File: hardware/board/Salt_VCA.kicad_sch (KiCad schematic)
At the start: 40 parts

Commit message: hardware: clear ERC issues, move BCM847 to the Winterbloom symbol library
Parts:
- Q?: symbol Carson's Schematic Symbols:BCM847 -> winterbloom:BCM847
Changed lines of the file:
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@@
     )
   )
-  (symbol (lib_name "BCM847_1") (lib_id "Carson's Schematic Symbols:BCM847") (at 161.29 140.97 270) (unit 1)
+  (symbol (lib_id "winterbloom:BCM847") (at 161.29 140.97 270) (unit 1)
     (in_bom yes) (on_board yes) (dnp no)
     (property "Reference" "Q?" (at 149.225 132.08 90)
@@
       (effects (font (size 1.27 1.27)) (justify left))
     )
-    (property "Footprint" "Package_TO_SOT_SMD:SOT-363_SC-70-6" (at 173.355 140.97 0)
+    (property "Footprint" "Package_TO_SOT_SMD:SOT-363_SC-70-6" (at 161.29 140.97 0)
       (effects (font (size 1.27 1.27)) hide)
     )
-    (property "Datasheet" "" (at 173.355 140.97 0)
+    (property "Datasheet" "https://assets.nexperia.com/documents/data-sheet/BCM847BS.pdf" (at 161.29 140.97 0)
       (effects (font (size 1.27 1.27)) hide)
     )

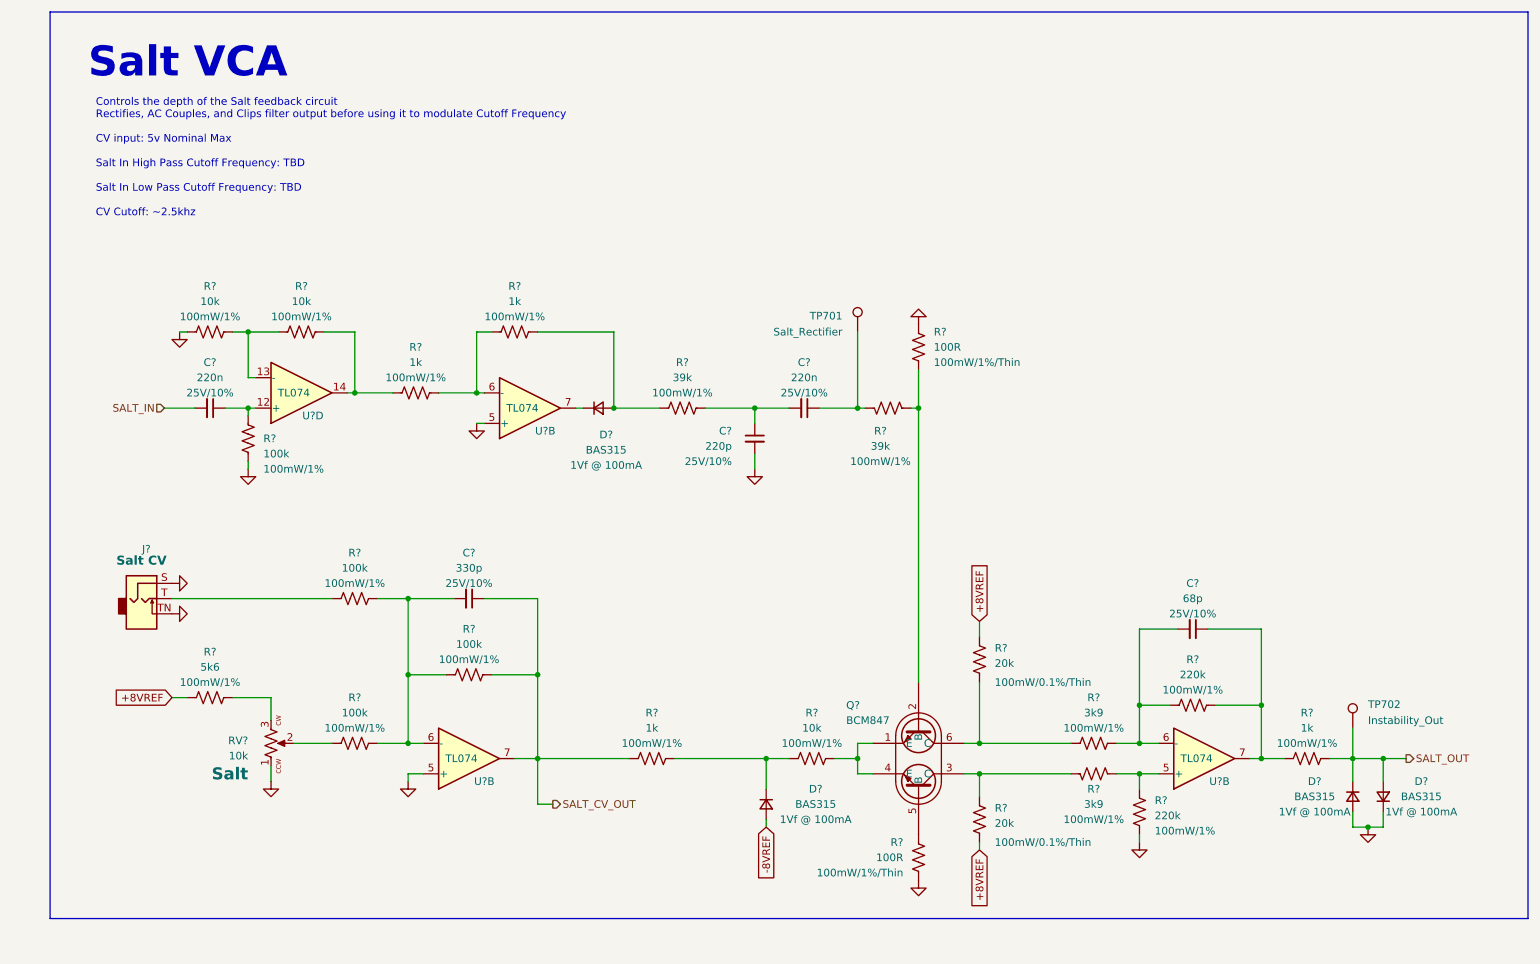
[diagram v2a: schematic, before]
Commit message: hardware: add MPNs, DigiKey part numbers, and LCSC part numbers for all BOM items
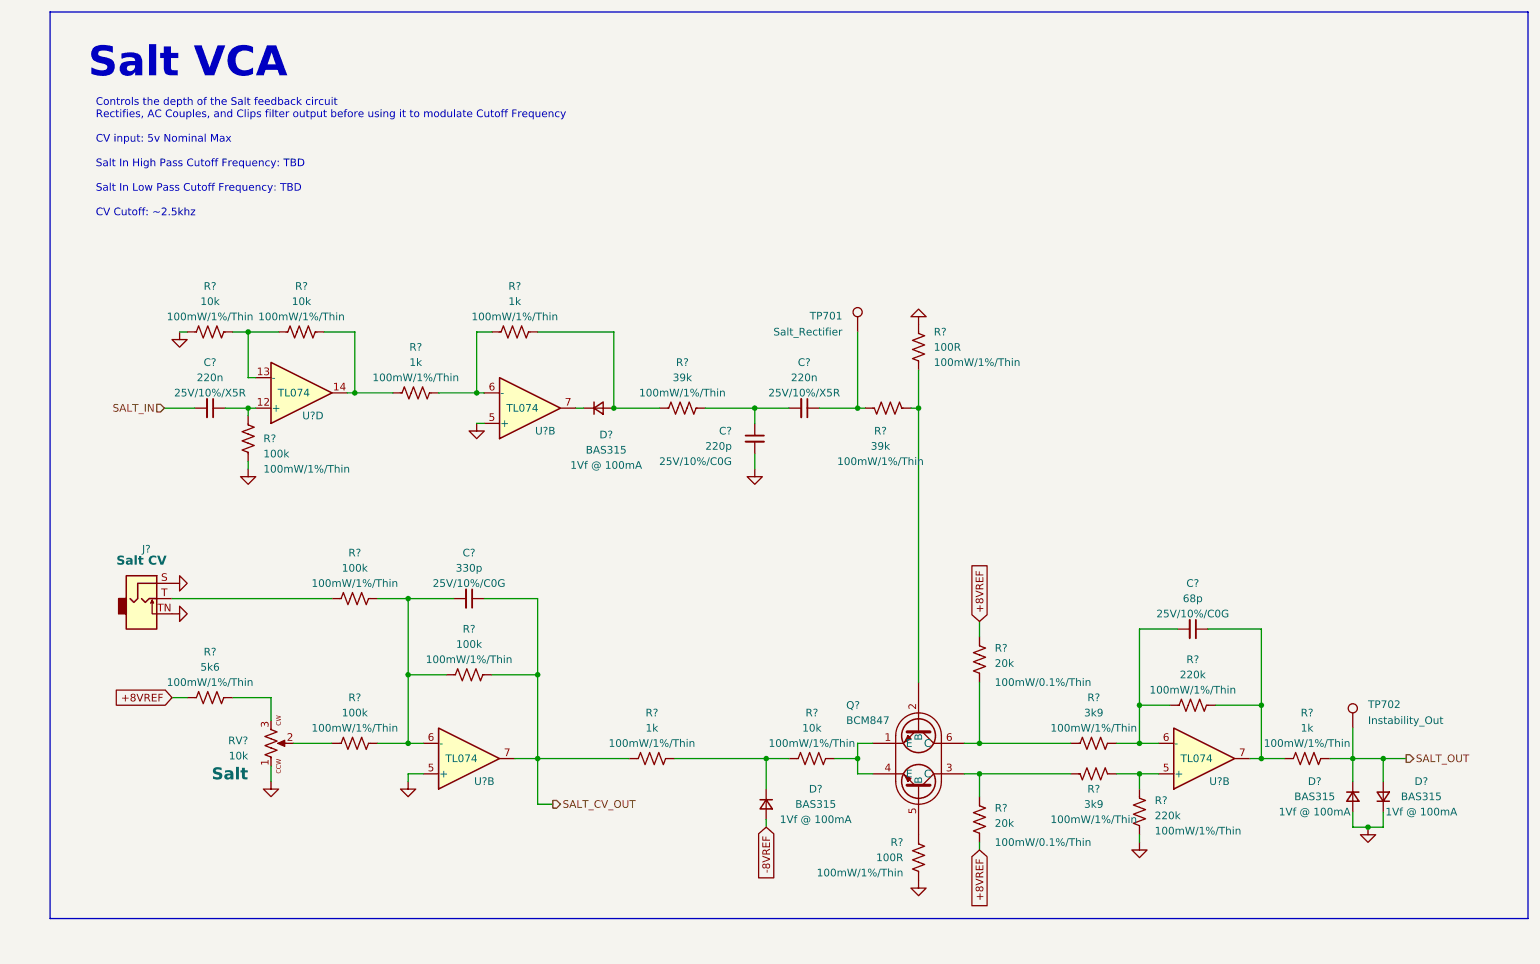
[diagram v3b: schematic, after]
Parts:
- C? (x2): DigiKey (none) -> 1276-1876-1-ND; LCSC (none) -> C307462; MPN (none) -> CL10A224KB8NNNC; Rating 25V/10% -> 25V/10%/X5R; Substitutes Allowed (none) -> Yes
- C?: DigiKey (none) -> 1276-1073-1-ND; LCSC (none) -> C1664; MPN (none) -> CL10C331JB8NNNC; Rating 25V/10% -> 25V/10%/C0G; Substitutes Allowed (none) -> Yes
- C?: DigiKey (none) -> 1276-1135-1-ND; LCSC (none) -> C28262; MPN (none) -> CL10C680JB8NNNC; Rating 25V/10% -> 25V/10%/C0G; Substitutes Allowed (none) -> Yes
- C?: DigiKey (none) -> 1276-1048-1-ND; LCSC (none) -> C27675; MPN (none) -> CL10C221JB8NNNC; Rating 25V/10% -> 25V/10%/C0G; Substitutes Allowed (none) -> Yes
- D? (x4): DigiKey (none) -> 1727-4309-2-ND; LCSC (none) -> C109218; Substitutes Allowed (none) -> No
- Q?: Attention ! -> (none); DigiKey (none) -> 1727-5456-1-ND; LCSC (none) -> C396099; Substitutes Allowed (none) -> No
- R? (x3): DigiKey (none) -> YAG2321CT-ND; LCSC (none) -> C469659; MPN (none) -> RT0603FRE0710KL; Rating 100mW/1% -> 100mW/1%/Thin; Substitutes Allowed (none) -> Yes
- R? (x2): DigiKey (none) -> YAG1582CT-ND; LCSC (none) -> C723637; MPN (none) -> RT0603BRD0720KL; Substitutes Allowed (none) -> Ask
- R? (x2): DigiKey (none) -> YAG1497CT-ND; LCSC (none) -> C122970; MPN (none) -> RT0603BRD07100RL; Substitutes Allowed (none) -> Ask
- R? (x2): DigiKey (none) -> YAG5961CT-ND; LCSC (none) -> C863790; MPN (none) -> RT0603FRE073K9L; Rating 100mW/1% -> 100mW/1%/Thin; Substitutes Allowed (none) -> Yes
- R? (x4): DigiKey (none) -> 13-RT0603FRE13100KLTR-ND; LCSC (none) -> C4107493; MPN (none) -> RT0603FRE13100KL; Rating 100mW/1% -> 100mW/1%/Thin; Substitutes Allowed (none) -> Yes
- R? (x4): DigiKey (none) -> YAG2323TR-ND; LCSC (none) -> C375503; MPN (none) -> RT0603FRE071KL; Rating 100mW/1% -> 100mW/1%/Thin; Substitutes Allowed (none) -> Yes
- R? (x2): DigiKey (none) -> 13-RT0603FRE0739KLCT-ND; LCSC (none) -> C706166; MPN (none) -> RT0603FRE0739KL; Rating 100mW/1% -> 100mW/1%/Thin; Substitutes Allowed (none) -> Yes
- R?: DigiKey (none) -> 13-RT0603FRE075K6LCT-ND; LCSC (none) -> C706186; MPN (none) -> RT0603FRE075K6L; Rating 100mW/1% -> 100mW/1%/Thin; Substitutes Allowed (none) -> Yes
- R? (x2): DigiKey (none) -> YAG5946CT-ND; LCSC (none) -> C706140; MPN (none) -> RT0603FRE07220KL; Rating 100mW/1% -> 100mW/1%/Thin; Substitutes Allowed (none) -> Yes
- U? (x4): DigiKey (none) -> 296-7198-1-ND; LCSC (none) -> C96507; MPN TL074CPW -> TL074CPWR; Substitutes Allowed (none) -> No

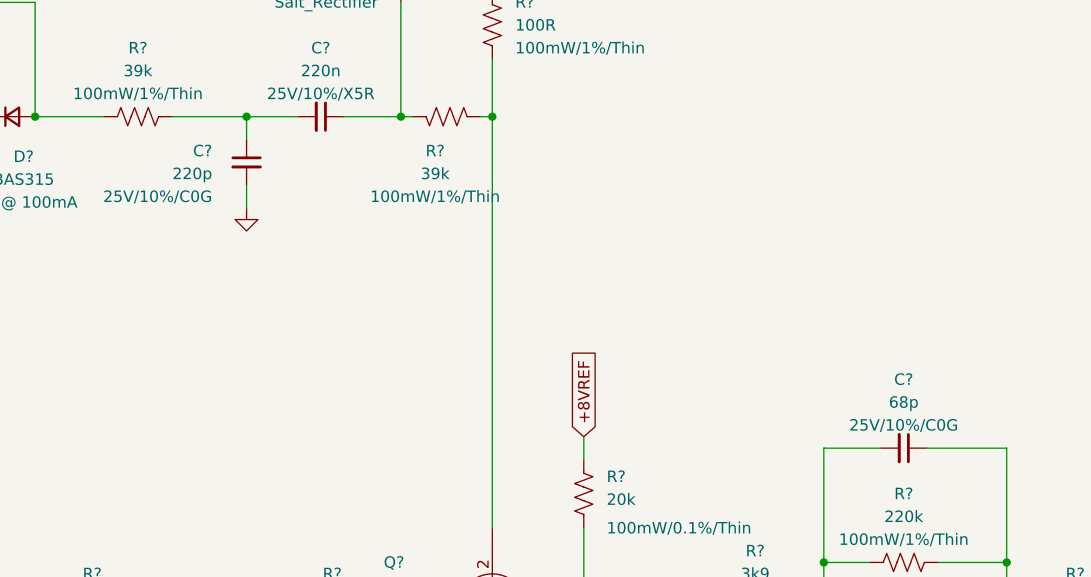
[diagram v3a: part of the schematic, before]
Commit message: hardware: change C702 from 220pF to 330pF and  C705 from 68pF to 100pF to reduce unique values
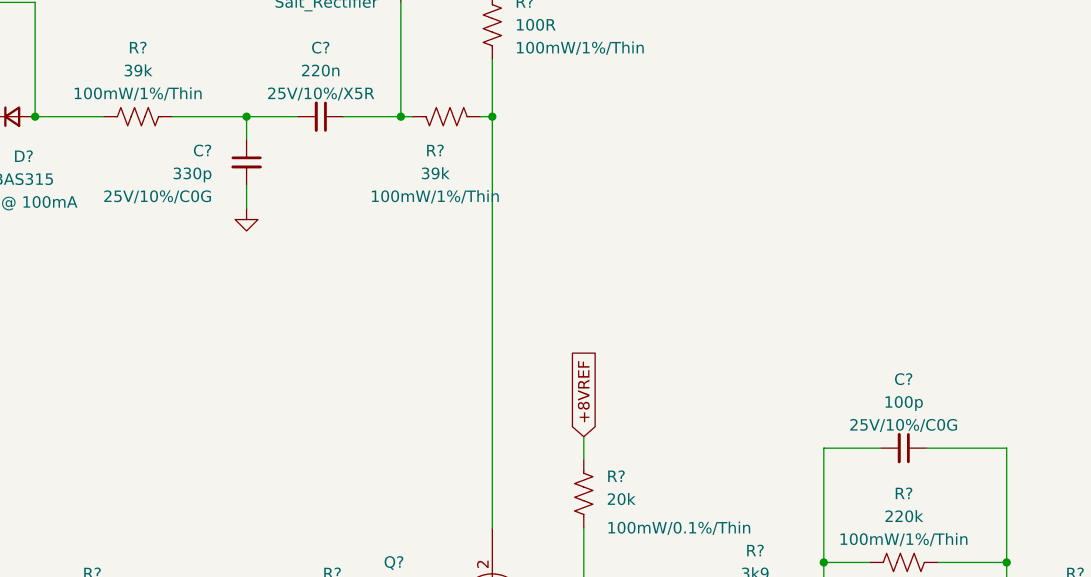
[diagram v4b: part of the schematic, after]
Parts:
- C?: value 68p -> 100p; DigiKey 1276-1135-1-ND -> 1276-1008-1-ND; LCSC C28262 -> C14858; MPN CL10C680JB8NNNC -> CL10C101JB8NNNC
- C?: value 220p -> 330p; DigiKey 1276-1048-1-ND -> 1276-1073-1-ND; LCSC C27675 -> C1664; MPN CL10C221JB8NNNC -> CL10C331JB8NNNC
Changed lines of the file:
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@@
       (effects (font (size 1.27 1.27)))
     )
-    (property "Value" "68p" (at 207.0036 114.3 90)
+    (property "Value" "100p" (at 207.0036 114.3 90)
       (effects (font (size 1.27 1.27)))
     )
@@
       (effects (font (size 1.27 1.27)))
     )
-    (property "DigiKey" "1276-1135-1-ND" (at 207.01 119.38 0)
-      (effects (font (size 1.27 1.27)) hide)
-    )
-    (property "LCSC" "C28262" (at 207.01 119.38 0)
+    (property "DigiKey" "1276-1008-1-ND" (at 207.01 119.38 0)
+      (effects (font (size 1.27 1.27)) hide)
+    )
+    (property "LCSC" "C14858" (at 207.01 119.38 0)
       (effects (font (size 1.27 1.27)) hide)
     )
@@
       (effects (font (size 1.27 1.27)) hide)
     )
-    (property "MPN" "CL10C680JB8NNNC" (at 207.01 119.38 0)
+    (property "MPN" "CL10C101JB8NNNC" (at 207.01 119.38 0)
       (effects (font (size 1.27 1.27)) hide)
     )
@@
       (effects (font (size 1.27 1.27)) (justify right))
     )
-    (property "Value" "220p" (at 130.175 88.9 0)
+    (property "Value" "330p" (at 130.175 88.9 0)
       (effects (font (size 1.27 1.27)) (justify right))
     )
@@
       (effects (font (size 1.27 1.27)) (justify right))
     )
-    (property "DigiKey" "1276-1048-1-ND" (at 133.985 87.63 0)
-      (effects (font (size 1.27 1.27)) hide)
-    )
-    (property "LCSC" "C27675" (at 133.985 87.63 0)
-      (effects (font (size 1.27 1.27)) hide)
-    )
-    (property "MPN" "CL10C221JB8NNNC" (at 133.985 87.63 0)
-      (effects (font (size 1.27 1.27)) hide)
-    )
+    (property "DigiKey" "1276-1073-1-ND" (at 133.985 87.63 0)
+      (effects (font (size 1.27 1.27)) hide)
+    )
+    (property "LCSC" "C1664" (at 133.985 87.63 0)
+      (effects (font (size 1.27 1.27)) hide)
+    )
+    (property "MPN" "CL10C331JB8NNNC" (at 133.985 87.63 0)
+      (effects (font (size 1.27 1.27)) hide)
+    )

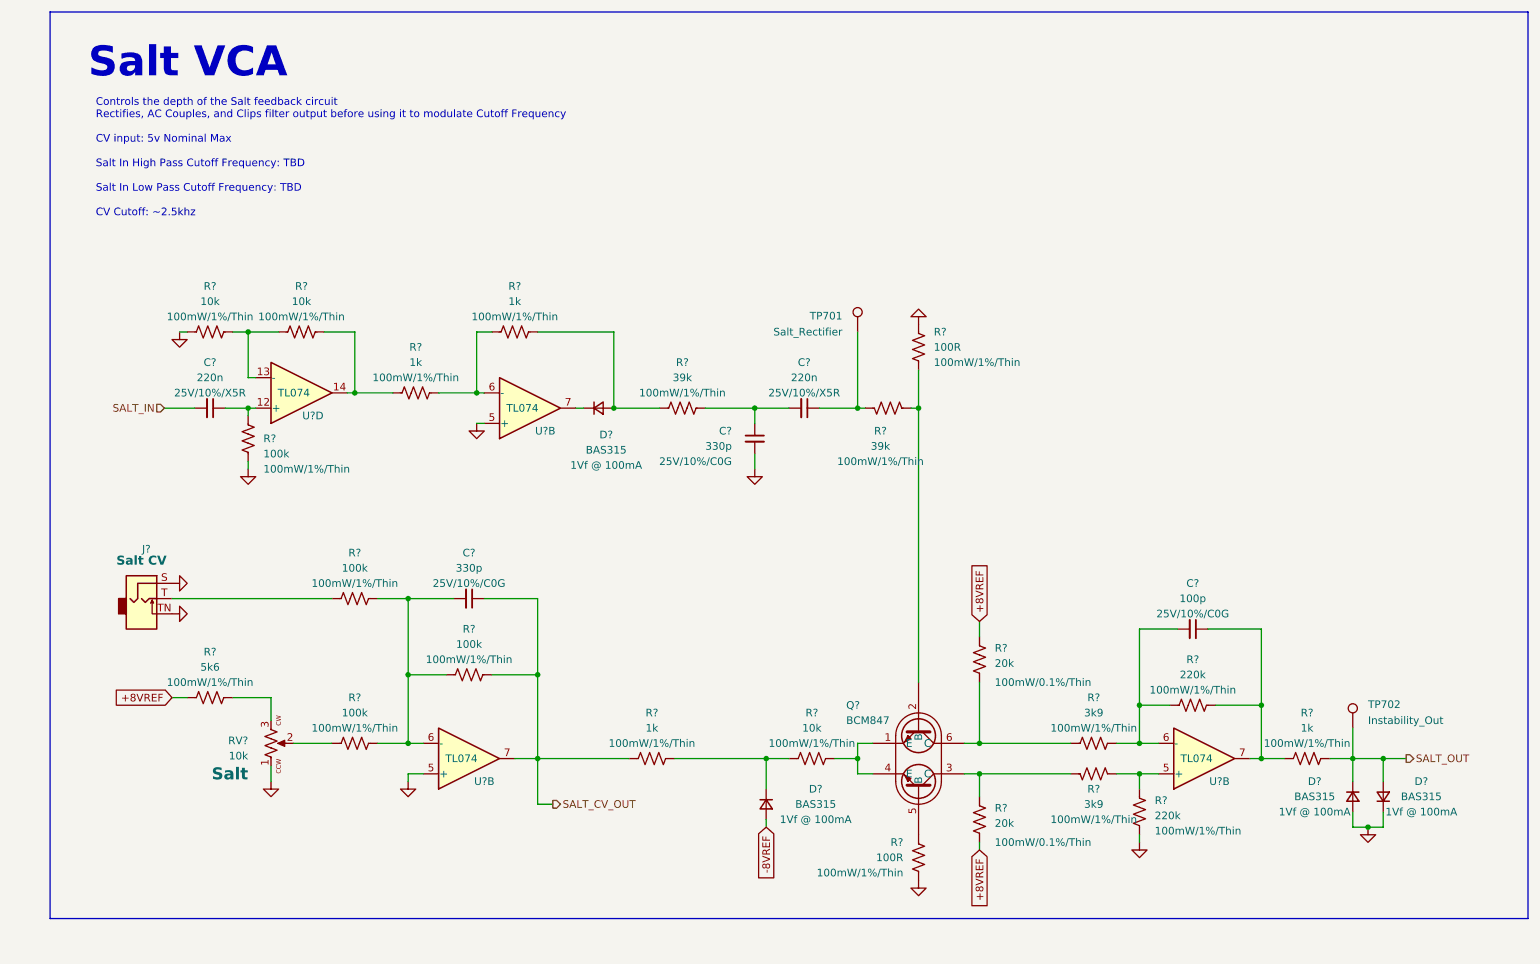
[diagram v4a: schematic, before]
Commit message: hardware: update schematic fonts/text sizes, some slight readability improvements
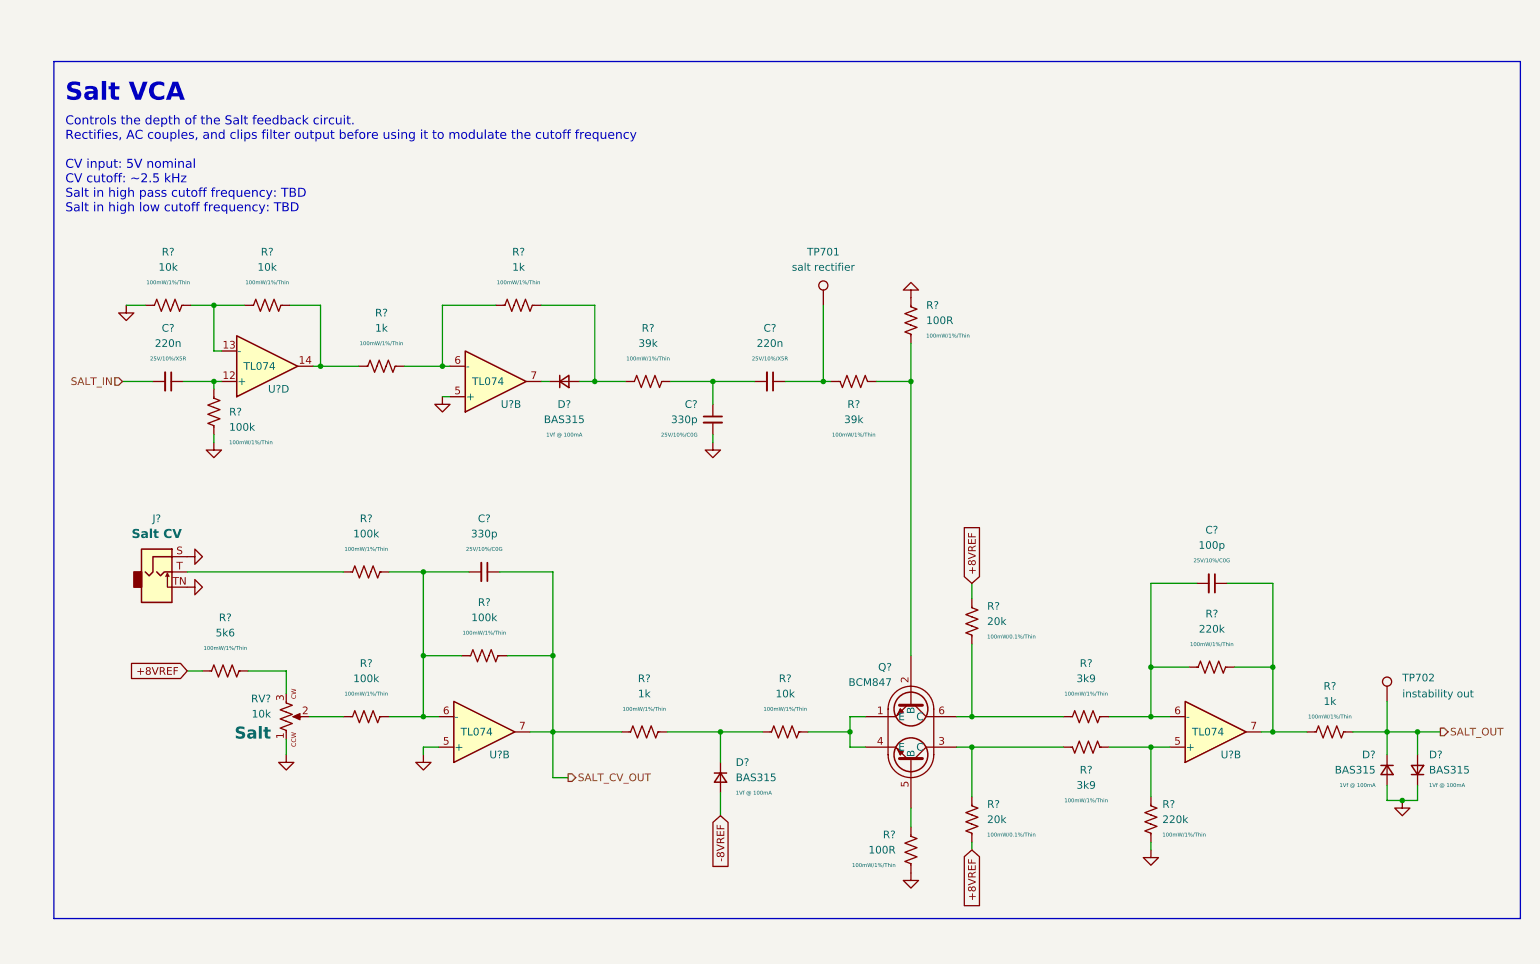
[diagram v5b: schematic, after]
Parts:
- TP701: Name Salt_Rectifier -> salt rectifier
- TP702: Name Instability_Out -> instability out
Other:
- note added: "Controls the depth of the Salt feedback circuit. Rectifies, AC couples, and clips filter output before using it to modulate the cutoff frequency CV input: 5V nominal CV cutoff: ~2.5 kHz Salt in high pass cutoff frequency: TBD Salt in high low cutoff frequency: TBD"
- note removed: "Controls the depth of the Salt feedback circuit Rectifies, AC Couples, and Clips filter output before using it to modulate Cutoff Frequency CV input: 5v Nominal Max Salt In High Pass Cutoff Frequency: TBD Salt In Low Pass Cutoff Frequency: TBD CV Cutoff: ~2.5khz"
- moved on the sheet: C?, D?, J?, Q?, R?, RV?, TP701, TP702, U?B, U?D
